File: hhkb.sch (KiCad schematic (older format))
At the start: 136 parts, among them J1 USB_mini_micro_B, SW1 SW_PUSH, U1 ATMEGA32U4, X1 XTAL_GND

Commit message: change usb connector footprint
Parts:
- J1: footprint keyboard_parts:USB_miniB_hirose_5ST_hand -> keyboard_parts:USB_miniB_hirose_5S8
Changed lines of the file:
@@
 F 0 "J1" H 4650 8000 60  0000 C CNN
 F 1 "USB_mini_micro_B" H 4900 8300 60  0001 C CNN
-F 2 "keyboard_parts:USB_miniB_hirose_5ST_hand" H 5000 8050 60  0001 C CNN
+F 2 "keyboard_parts:USB_miniB_hirose_5S8" H 5000 8050 60  0001 C CNN
 F 3 "" H 5000 8050 60  0000 C CNN
 	1    5050 8050

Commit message: Done
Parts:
- removed D1:1: D, Diodes_SMD:D_SOD-123, symbol D
- removed ESC1: KEYSW, TheKeebrary:MX_Plate_100H, symbol KEYSW
- "'"1, ","1, "-"1, "."1, "/"1, "0"1, "1"1, "2"1, "3"1, "4"1, "5"1, "6"1, "7"1, "8"1, "9"1, ";"1, "="1, "A"1, "B"1, "C"1, "D"1, "E"1, "F"1, "G"1, "H"1, "I"1, "J"1, "K"1, "L"1, "M"1, "N"1, "O"1, "P"1, "Q"1, "R"1, "S"1, "T"1, "U"1, "V"1, "W"1, "X"1, "Y"1, "Z"1, "["1, "\"1, "]"1, "`"1, ALT1, R_ALT1, R_FN1: footprint TheKeebrary:MX_Plate_100H -> AlpsKeys:Alps100
- BS1, L_CMD1, R_CMD1: footprint TheKeebrary:MX_Plate_150H -> AlpsKeys:Alps150
- CTRL1: footprint TheKeebrary:MX_Plate_175H -> AlpsKeys:Alps100
- D10:10, D10:11, D10:12, D10:7, D10:8, D10:9, D1:3, D1:4, D1:5, D1:6, D2:1, D2:2, D2:3, D2:4, D2:5, D2:6, D3:1, D3:2, D3:3, D3:4, D3:5, D3:6, D4:1, D4:2, D4:3, D4:4, D4:5, D4:6, D5:1, D5:2, D5:3, D5:4, D5:5, D5:6, D6:12, D6:7, D6:8, D6:9, D7:10, D7:11, D7:12, D7:8, D7:9, D8:10, D8:11, D8:12, D8:7, D8:8, D8:9, D9:10, D9:11, D9:12, D9:7, D9:8, D9:9, D:6:10, D:6:11, D:7:7: footprint Diodes_SMD:D_SOD-123 -> Diodes_THT:D_T-1_P12.70mm_Horizontal
- D1:2: footprint Diodes_SMD:D_SOD-123 -> Diodes_THT:D_T-1_P10.16mm_Horizontal
- L_SHIFT1, RET1: footprint TheKeebrary:MX_Plate_225H -> AlpsKeys:Alps150
- R_SHIFT1: footprint TheKeebrary:MX_Plate_175H -> AlpsKeys:Alps150
- SPACEBAR1: footprint TheKeebrary:MX_Plate_600H_Stepped -> AlpsKeys:Alps600
- TAB1: footprint TheKeebrary:MX_Plate_150H -> AlpsKeys:Alps100
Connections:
- net COL1: now also U1.40 (PF1); no longer U1.8 (PB0/SS)
- net COL10: now also U1.29 (PB5); no longer U1.36 (PF7)
- net COL11: now also U1.25 (ICP1/PD4); no longer U1.37 (PF6)
- net COL12: now also U1.8 (PB0/SS); no longer U1.38 (PF5)
- net COL2: now also U1.41 (PF0); no longer U1.9 (PB1/SCK)
- net COL4: now also U1.31 (PC6); no longer U1.20 (PD2/RXD1)
- net COL5: now also U1.18 (PD0/INT0); no longer U1.21 (PD3/TXD1)
- net COL6: now also U1.12 (PB7/~RTS); no longer U1.22 (PD5/XCK1)
- net COL7: now also U1.11 (PB3/MISO); no longer U1.28 (PB4)
- net COL8: now also U1.26 (T1/PD6); no longer U1.29 (PB5)
- net COL9: now also U1.30 (PB6); no longer U1.31 (PC6)
- net ROW1: now also U1.22 (PD5/XCK1); no longer U1.27 (T0/PD7)
- net ROW10: now also U1.28 (PB4); no longer U1.30 (PB6)
- net ROW2: now also U1.32 (PC7); no longer U1.26 (T1/PD6)
- net ROW3: now also U1.38 (PF5); no longer U1.25 (ICP1/PD4)
- net ROW4: now also U1.37 (PF6); no longer U1.12 (PB7/~RTS)
- net ROW5: now also U1.39 (PF4); no longer U1.11 (PB3/MISO)
- net ROW6: now also U1.19 (PD1/INT1); no longer U1.41 (PF0)
- net ROW7: now also U1.20 (PD2/RXD1); no longer U1.40 (PF1)
- net ROW8: now also U1.21 (PD3/TXD1); no longer U1.39 (PF4)
- net ROW9: now also U1.27 (T0/PD7); no longer U1.32 (PC7)
- no-connect marks 5 -> 3

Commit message: Rework from scratch
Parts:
- renumbered D1:2 to D1:1, D6:8 to D1:10, D6:9 to D1:11, D:6:10 to D1:12, D:6:11 to D1:13, D6:12 to D1:14, D1:3 to D1:2, D1:4 to D1:3, D1:5 to D1:4, D1:6 to D1:5, D2:6 to D1:6, D8:7 to D1:7, D:7:7 to D1:8, D6:7 to D1:9, D7:8 to D2:10, D7:9 to D2:11, D7:10 to D2:12, D7:11 to D2:13, D7:12 to D2:14, D3:6 to D2:6, D4:6 to D2:7, D9:7 to D2:8, D8:8 to D2:9, D8:9 to D3:10, D8:10 to D3:11, D8:11 to D3:12, D8:12 to D3:13, D4:5 to D3:6, D5:5 to D3:7, D10:7 to D3:8, D9:8 to D3:9, D5:1 to D4:1, D9:9 to D4:10, D9:10 to D4:11, D9:11 to D4:12, D9:12 to D4:13, D4:1 to D4:2, D4:2 to D4:3, D4:3 to D4:4, D4:4 to D4:5, D5:4 to D4:6, D10:8 to D4:7, D10:9 to D4:8, D10:10 to D4:9, D10:11 to D5:10, D10:12 to D5:11
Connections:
- net labels added: COL13, COL14
- net labels removed: ROW10, ROW6, ROW7, ROW8, ROW9
- wire segments 195 -> 317
- no-connect marks 3 -> 5
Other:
- moved on the sheet: "'"1, ","1, "-"1, "."1, "/"1, "0"1, "1"1, "2"1, "3"1, "4"1, "5"1, "6"1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

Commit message: redraw
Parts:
- D1:10, D1:11, D1:12, D1:2, D1:3, D1:4, D1:5, D1:8, D1:9, D2:1, D2:10, D2:11, D2:12, D2:13, D2:14, D2:2, D2:3, D2:4, D2:5, D2:6, D2:7, D2:8, D2:9, D3:1, D3:10, D3:11, D3:12, D3:13, D3:2, D3:3, D3:4, D3:5, D3:6, D3:7, D3:8, D3:9, D4:1, D4:10, D4:11, D4:12, D4:13, D4:2, D4:3, D4:4, D4:5, D4:6, D4:7, D4:8, D4:9, D5:10, D5:11, D5:2, D5:3, D5:6: footprint Diodes_THT:D_T-1_P12.70mm_Horizontal -> Diodes_THT:D_T-1_P10.16mm_Horizontal
- D1:13, D1:14, D1:6, D1:7: footprint Diodes_THT:D_T-1_P12.70mm_Horizontal -> Diodes_THT:D_T-1_P5.08mm_Horizontal
- J1: footprint keyboard_parts:USB_miniB_hirose_5S8 -> keyboard_parts:USB_miniB_hirose_5ST_hand
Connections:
- net labels added: ROW6
- net labels removed: COL14
- wire segments 317 -> 316
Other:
- moved on the sheet: "`"1, BS1, D1:14, D2:14, D3:13, D4:12, D4:13, RET1, R_FN1, R_SHIFT1

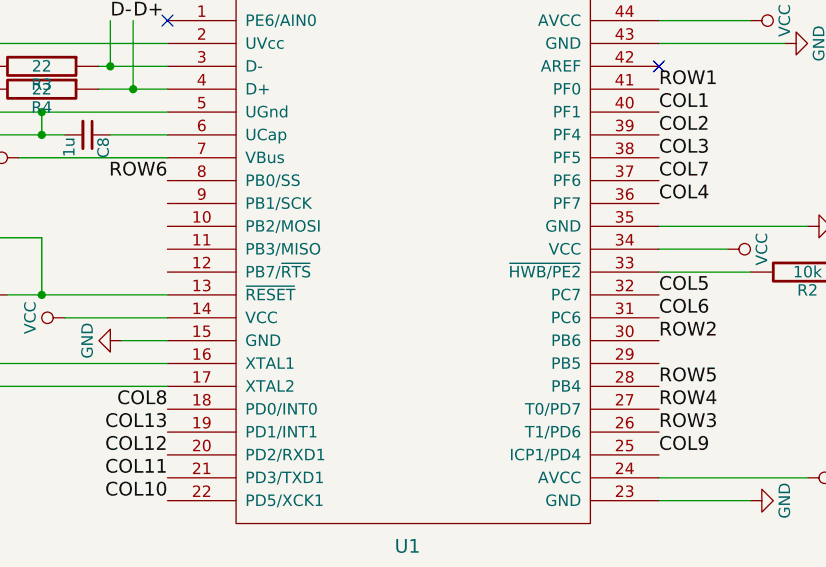
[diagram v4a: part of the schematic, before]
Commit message: Change usb footprint
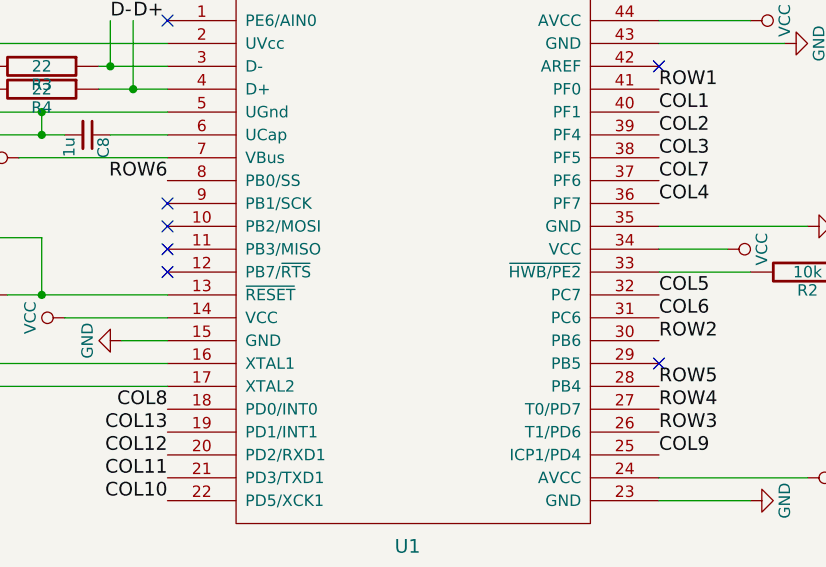
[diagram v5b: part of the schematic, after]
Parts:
- J1: footprint keyboard_parts:USB_miniB_hirose_5ST_hand -> keyboard_parts:USB_miniB_through_hole
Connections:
- no-connect marks 5 -> 10
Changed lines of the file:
@@
 F 0 "J1" H 4650 8000 60  0000 C CNN
 F 1 "USB_mini_micro_B" H 4900 8300 60  0001 C CNN
-F 2 "keyboard_parts:USB_miniB_hirose_5ST_hand" H 5000 8050 60  0001 C CNN
+F 2 "keyboard_parts:USB_miniB_through_hole" H 5000 8050 60  0001 C CNN
 F 3 "" H 5000 8050 60  0000 C CNN
 	1    5050 8050
@@
 Wire Wire Line
 	6000 9200 6200 9200
-Wire Wire Line
-	6300 10800 6200 10800
-Wire Wire Line
-	6300 10700 6200 10700
-Wire Wire Line
-	6300 10600 6200 10600
-Wire Wire Line
-	6300 10500 6200 10500
-Wire Wire Line
-	6300 10400 6200 10400
 Connection ~ 7850 1800
 Connection ~ 4650 1800
@@
 Text Label 6200 8500 2    60   ~ 0
 ROW6
+Wire Wire Line
+	6300 10400 6200 10400
+Wire Wire Line
+	6300 10500 6200 10500
+Wire Wire Line
+	6300 10600 6200 10600
+Wire Wire Line
+	6300 10700 6200 10700
+Wire Wire Line
+	6300 10800 6200 10800
+NoConn ~ 6200 8600
+NoConn ~ 6200 8700
+NoConn ~ 6200 8800
+NoConn ~ 6200 8900
+NoConn ~ 8350 9300
 $EndSCHEMATC

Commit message: Gen gerbers
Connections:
- wire segments 316 -> 311
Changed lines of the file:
@@
 Text Label 6200 8500 2    60   ~ 0
 ROW6
-Wire Wire Line
-	6300 10400 6200 10400
-Wire Wire Line
-	6300 10500 6200 10500
-Wire Wire Line
-	6300 10600 6200 10600
-Wire Wire Line
-	6300 10700 6200 10700
-Wire Wire Line
-	6300 10800 6200 10800
 NoConn ~ 6200 8600
 NoConn ~ 6200 8700
